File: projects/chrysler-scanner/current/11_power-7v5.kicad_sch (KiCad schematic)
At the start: 15 parts, among them U7 LMR14010, U8 TLV76701DRV

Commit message: Use native ground symbols and document companion app feasibility
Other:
- note added: "All TLV767 ground terminals and exposed pads connect to GND in this checked revision."
- note added: "Native schematic and PCB ground connectivity are checked in the final validation reports."
- note removed: "REVIEW: U8 pin 5 is NC in the source; TLV767 DRV requires GND."
- note removed: "Source connectivity is preserved here. Correct this in atopile before routing."

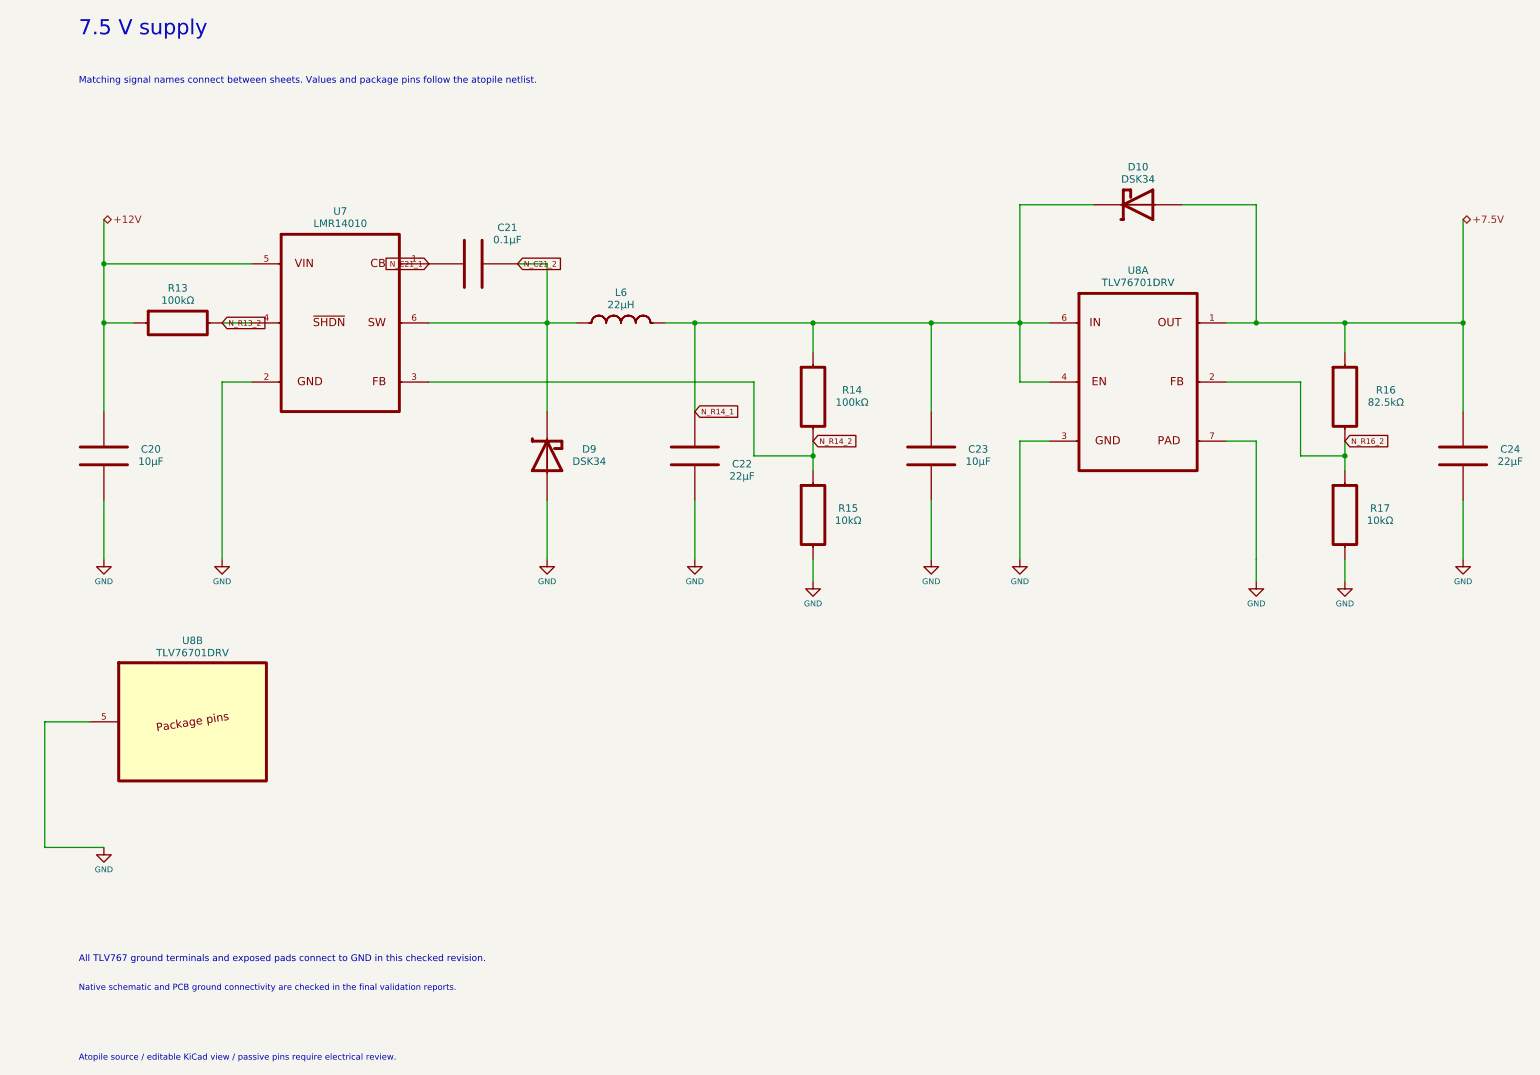
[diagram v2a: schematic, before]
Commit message: Fix scanner protection, ADC isolation and health watchdog
Coordinate the bounded 12 V input clamp and programming FET/capacitor ratings, add powered-off ADC isolation, and supervise the AW9523B permit with a dedicated GPIO13 health heartbeat. Preserve original placements and document all deliberate source-PDF deviations.

Validation: native ERC and full DRC/parity/refill report zero findings; strict preservation/connectivity audit and final adversarial review pass within the documented prototype bounds. Regenerate Rev C PDF, BOM, manufacturing exports, processing sites and verified portable archives. Compatible firmware and bench/mechanical qualification remain required.
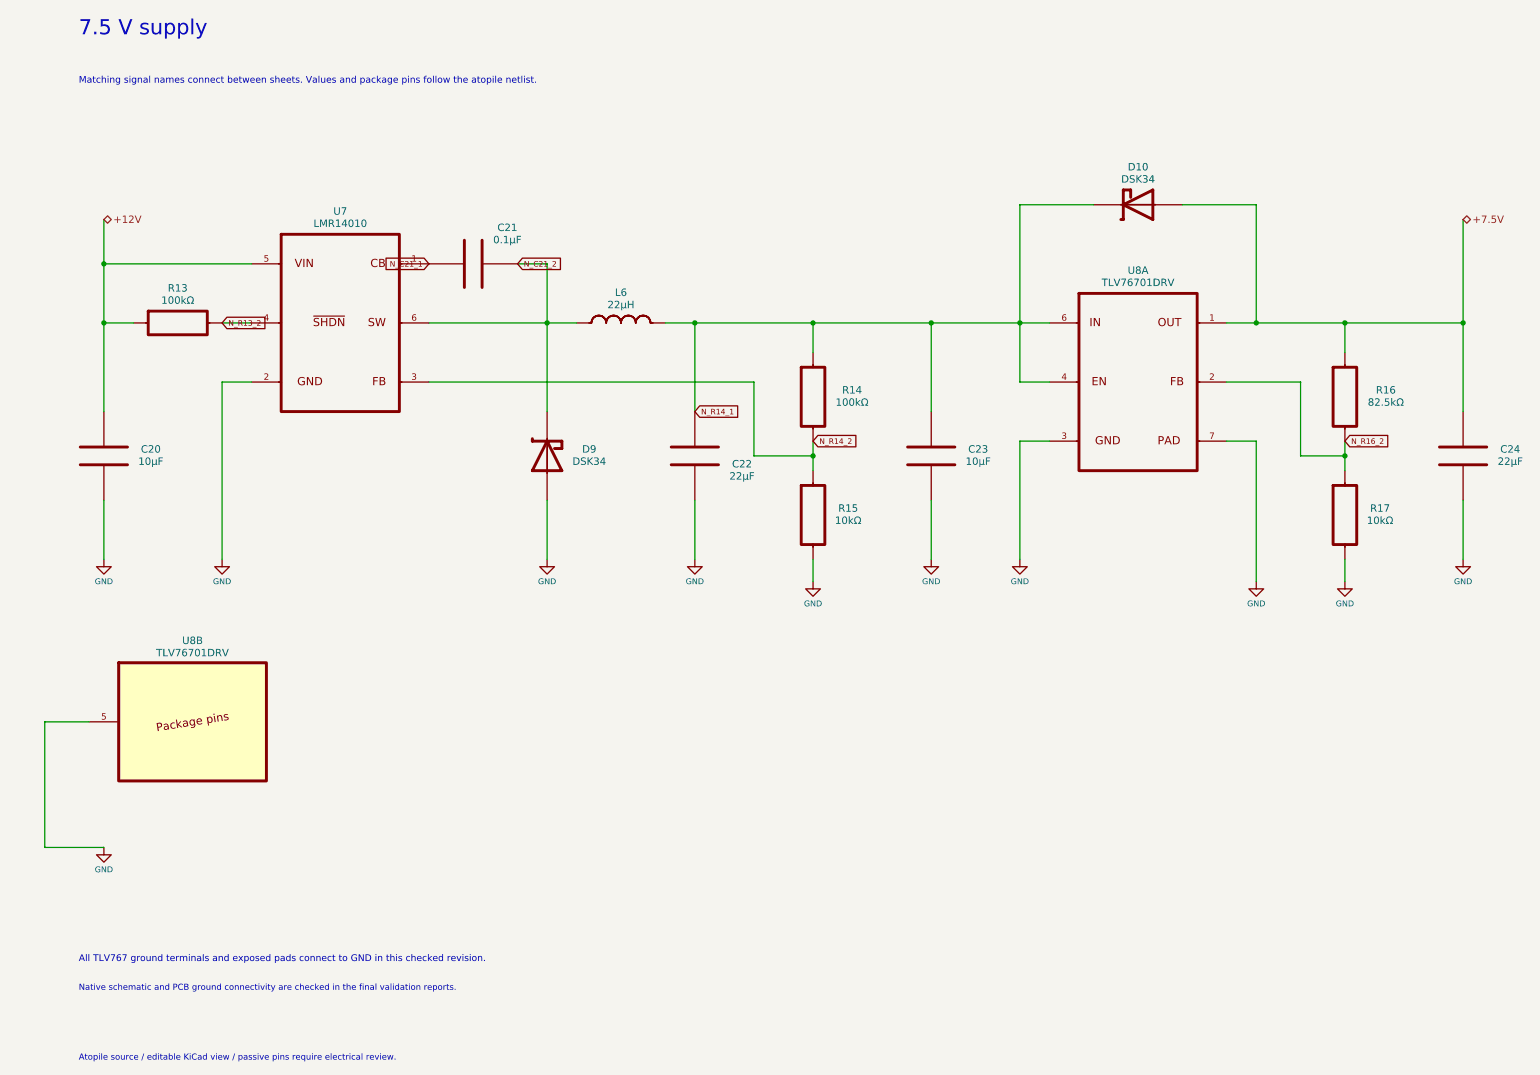
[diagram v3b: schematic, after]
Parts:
- C20: Voltage Rating (none) -> 50V
- C21: Voltage Rating (none) -> 100V
- C22, C23, C24: Voltage Rating (none) -> 25V

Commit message: Restore schematic polarity and visible capacitor ratings
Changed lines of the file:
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@@
 			)
 		)
-	(property "Voltage Rating" "50V" (at 0 0 0) (effects (font (size 1 1)) (hide yes))))
+	(property "Voltage Rating" "50V" (at 28.3959 94.49 0) (effects (font (size 1 1)))))
 	(symbol
 		(lib_id "power:GND")
@@
 			)
 		)
-	(property "Voltage Rating" "25V" (at 0 0 0) (effects (font (size 1 1)) (hide yes))))
+	(property "Voltage Rating" "25V" (at 130.029 97.03 0) (effects (font (size 1 1)))))
 	(symbol
 		(lib_id "power:GND")
@@
 			)
 		)
-	(property "Voltage Rating" "100V" (at 0 0 0) (effects (font (size 1 1)) (hide yes))))
+	(property "Voltage Rating" "100V" (at 89.6886 56.39 0) (effects (font (size 1 1)))))
 	(symbol
 		(lib_id "ChryslerScanner:R16")
@@
 			)
 		)
-	(property "Voltage Rating" "25V" (at 0 0 0) (effects (font (size 1 1)) (hide yes))))
+	(property "Voltage Rating" "25V" (at 262.109 94.49 0) (effects (font (size 1 1)))))
 	(symbol
 		(lib_id "power:GND")
@@
 			)
 		)
-	(property "Voltage Rating" "25V" (at 0 0 0) (effects (font (size 1 1)) (hide yes))))
+	(property "Voltage Rating" "25V" (at 170.636 94.49 0) (effects (font (size 1 1)))))
 	(symbol
 		(lib_id "power:GND")

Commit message: Finish Chrysler scanner CCD correction and procurement fabrication package
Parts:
- C20, C23: Assembly (none) -> PLACE; MPN (none) -> CGA5L1X7R1H106K160AC; Manufacturer (none) -> TDK; Procurement Source (none) -> https://product.tdk.com/info/en/documents/chara_sheet/CGA5L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; Selected Voltage Rating (none) -> 50V; Tolerance (none) -> 10%
- C21: Assembly (none) -> PLACE; MPN (none) -> C1206C104K1RACTU; Manufacturer (none) -> KEMET; Procurement Source (none) -> https://search.kemet.com/component-documentation/download/s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; Selected Voltage Rating (none) -> 100V; Tolerance (none) -> 10%
- C22, C24: Assembly (none) -> PLACE; MPN (none) -> C3216X5R1E226M160AB; Manufacturer (none) -> TDK; Procurement Source (none) -> https://product.tdk.com/en/search/capacitor/ceramic/mlcc/in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; Selected Voltage Rating (none) -> 25V; Tolerance (none) -> 20%
- D10, D9: Assembly (none) -> PLACE; MPN (none) -> DSK34; Manufacturer (none) -> MDD (Microdiode Electronics); Procurement Source (none) -> https://datasheet.lcsc.com/lcsc/DSK34_C41029.pdf
- L6: footprint footprints:L_7.3x7.3_H3.5 -> footprints:L_Eaton_DR74_220_R; Assembly (none) -> PLACE; MPN (none) -> DR74-220-R; Manufacturer (none) -> Eaton; Model Representation (none) -> Representative maximum overall envelope; Fab/courtyard and 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; Procurement Source (none) -> https://www.eaton.com/us/en-us/skuPage.DR74-220-R.html; Selected Height (none) -> 4.35mm max
- R13: Assembly (none) -> PLACE; MPN (none) -> CRCW0603100KFKEA; Manufacturer (none) -> Vishay; Procurement Source (none) -> https://www.vishay.com/docs/20035/dcrcwe3.pdf; Selected Power Rating (none) -> 0.1W; Tolerance (none) -> 1%
- R14: Assembly (none) -> PLACE; MPN (none) -> TNPW0603100KBEEA; Manufacturer (none) -> Vishay; Procurement Source (none) -> https://www.vishay.com/docs/28758/tnpw_e3.pdf; Selected Power Rating (none) -> 0.1W; Tolerance (none) -> 0.1%
- R15, R17: Assembly (none) -> PLACE; MPN (none) -> TNPW060310K0BEEA; Manufacturer (none) -> Vishay; Procurement Source (none) -> https://www.vishay.com/docs/28758/tnpw_e3.pdf; Selected Power Rating (none) -> 0.1W; Tolerance (none) -> 0.1%
- R16: Assembly (none) -> PLACE; MPN (none) -> TNPW060382K5BEEA; Manufacturer (none) -> Vishay; Procurement Source (none) -> https://www.vishay.com/docs/28758/tnpw_e3.pdf; Selected Power Rating (none) -> 0.1W; Tolerance (none) -> 0.1%
- U7: Assembly (none) -> PLACE; MPN (none) -> LMR14010ADDCR; Manufacturer (none) -> Texas Instruments; Procurement Source (none) -> https://www.ti.com/lit/ds/symlink/lmr14010a.pdf
- U8: Assembly (none) -> PLACE; MPN (none) -> TLV76701DRVR; Manufacturer (none) -> Texas Instruments; Procurement Source (none) -> https://www.ti.com/lit/ds/symlink/tlv767.pdf

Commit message: Refine programming drive, Eaton lands and mounting clearance
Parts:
- L6: footprint footprints:L_Eaton_DR74_220_R -> footprints:L_Eaton_DR74_Recommended
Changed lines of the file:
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@@
 			)
 		)
-		(property "Footprint" "footprints:L_Eaton_DR74_220_R"
+		(property "Footprint" "footprints:L_Eaton_DR74_Recommended"
 			(at 109.22 68.58 0)
 			(hide yes)
